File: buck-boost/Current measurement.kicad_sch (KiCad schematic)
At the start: 15 parts, among them U3 ACS712ELCTR-20A, U8 ACS730xLCTR-20AB, U9 ACS712ELCTR-20A

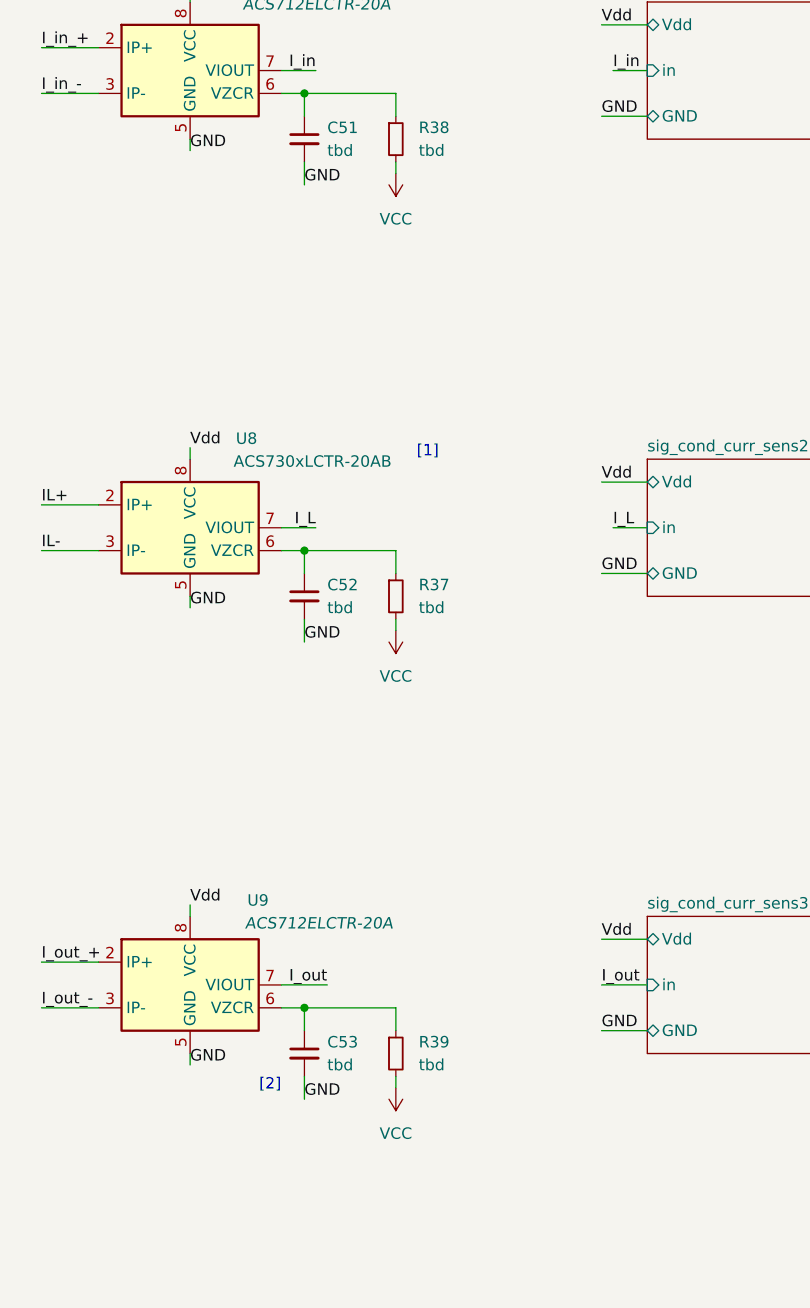
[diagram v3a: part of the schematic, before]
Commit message: Some errors in the schematics were corrected. PCB file V1.0
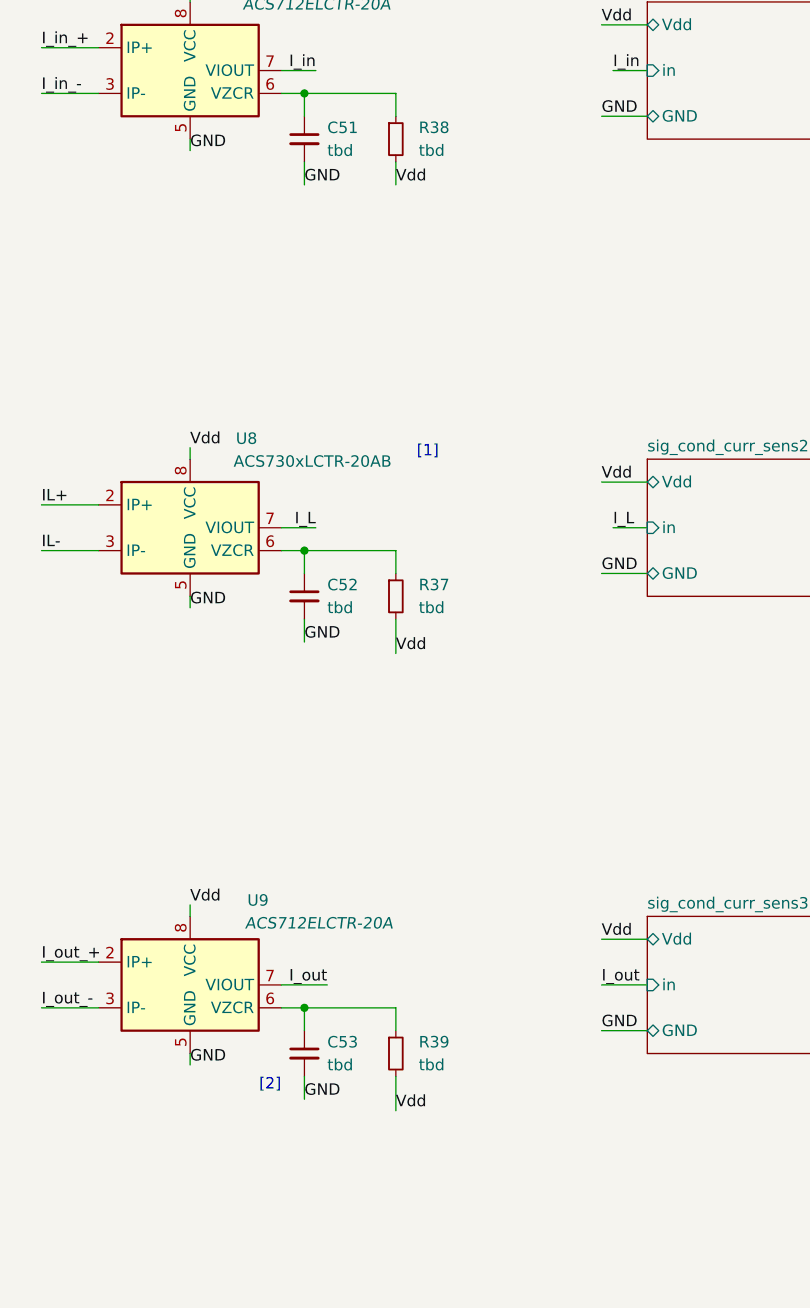
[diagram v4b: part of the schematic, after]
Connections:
- net VCC is gone; now on net Vdd: R37.2, R38.2, R39.2
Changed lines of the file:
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@@
-	(wire
-		(pts
-			(xy 116.84 142.24) (xy 116.84 143.51)
-		)
-		(stroke
-			(width 0)
-			(type default)
-		)
-	)
 	(wire
 		(pts
@@
 	(wire
 		(pts
-			(xy 116.84 91.44) (xy 116.84 92.71)
+			(xy 116.84 91.44) (xy 116.84 95.25)
 		)
 		(stroke
@@
 	(wire
 		(pts
+			(xy 116.84 142.24) (xy 116.84 146.05)
+		)
+		(stroke
+			(width 0)
+			(type default)
+		)
+	)
+	(wire
+		(pts
 			(xy 39.37 85.09) (xy 50.8 85.09)
 		)
@@
 	(wire
 		(pts
-			(xy 116.84 40.64) (xy 116.84 41.91)
+			(xy 116.84 40.64) (xy 116.84 43.18)
 		)
 		(stroke
@@
 		)
 	)
+	(label "Vdd"
+		(at 116.84 43.18 0)
+		(fields_autoplaced yes)
+		(effects
+			(font
+				(size 1.27 1.27)
+			)
+			(justify left bottom)
+		)
+	)
 	(label "IL_sens"
 		(at 74.93 180.34 0)
@@
 	(label "I_in_+"
 		(at 50.8 177.8 0)
+		(fields_autoplaced yes)
+		(effects
+			(font
+				(size 1.27 1.27)
+			)
+			(justify left bottom)
+		)
+	)
+	(label "Vdd"
+		(at 116.84 146.05 0)
+		(fields_autoplaced yes)
+		(effects
+			(font
+				(size 1.27 1.27)
+			)
+			(justify left bottom)
+		)
+	)
+	(label "Vdd"
+		(at 116.84 95.25 0)
 		(fields_autoplaced yes)
 		(effects
@@
 				(path "/3f994017-d36f-4c43-a8c8-740bd919e8ad/70cf8e5f-42f7-4af1-be5f-f7a395e09e78/4c95cbf9-e4e0-409d-a846-0f8d58b8f8d6"
 					(reference "R39")
-					(unit 1)
-				)
-			)
-		)
-	)
-	(symbol
-		(lib_id "power:VCC")
-		(at 116.84 92.71 180)
-		(unit 1)
-		(exclude_from_sim no)
-		(in_bom yes)
-		(on_board yes)
-		(dnp no)
-		(fields_autoplaced yes)
-		(property "Reference" "#PWR024"
-			(at 116.84 88.9 0)
-			(effects
-				(font
-					(size 1.27 1.27)
-				)
-				(hide yes)
-			)
-		)
-		(property "Value" "VCC"
-			(at 116.84 97.79 0)
-			(effects
-				(font
-					(size 1.27 1.27)
-				)
-			)
-		)
-		(property "Footprint" ""
-			(at 116.84 92.71 0)
-			(effects
-				(font
-					(size 1.27 1.27)
-				)
-				(hide yes)
-			)
-		)
-		(property "Datasheet" ""
-			(at 116.84 92.71 0)
-			(effects
-				(font
-					(size 1.27 1.27)
-				)
-				(hide yes)
-			)
-		)
-		(property "Description" "Power symbol creates a global label with name \"VCC\""
-			(at 116.84 92.71 0)
-			(effects
-				(font
-					(size 1.27 1.27)
-				)
-				(hide yes)
-			)
-		)
-		(pin "1"
-		)
-		(instances
-			(project "buck-boost-xp"
-				(path "/3f994017-d36f-4c43-a8c8-740bd919e8ad/70cf8e5f-42f7-4af1-be5f-f7a395e09e78/4c95cbf9-e4e0-409d-a846-0f8d58b8f8d6"
-					(reference "#PWR024")
 					(unit 1)
 				)
@@
 					(unit 1)
 				)
-			)
-		)
-	)
-	(symbol
-		(lib_id "power:VCC")
-		(at 116.84 41.91 180)
-		(unit 1)
-		(exclude_from_sim no)
-		(in_bom yes)
-		(on_board yes)
-		(dnp no)
-		(fields_autoplaced yes)
-		(property "Reference" "#PWR022"
-			(at 116.84 38.1 0)
-			(effects
-				(font
-					(size 1.27 1.27)
-				)
-				(hide yes)
-			)
-		)
-		(property "Value" "VCC"
-			(at 116.84 46.99 0)
-			(effects
-				(font
-					(size 1.27 1.27)
-				)
-			)
-		)
-		(property "Footprint" ""
-			(at 116.84 41.91 0)
-			(effects
-				(font
-					(size 1.27 1.27)
-				)
-				(hide yes)
-			)
-		)
-		(property "Datasheet" ""
-			(at 116.84 41.91 0)
-			(effects
-				(font
-					(size 1.27 1.27)
-				)
-				(hide yes)
-			)
-		)
-		(property "Description" "Power symbol creates a global label with name \"VCC\""
-			(at 116.84 41.91 0)
-			(effects
-				(font
-					(size 1.27 1.27)
-				)
-				(hide yes)
-			)
-		)
-		(pin "1"
-		)
-		(instances
-			(project "buck-boost-xp"
-				(path "/3f994017-d36f-4c43-a8c8-740bd919e8ad/70cf8e5f-42f7-4af1-be5f-f7a395e09e78/4c95cbf9-e4e0-409d-a846-0f8d58b8f8d6"
-					(reference "#PWR022")
-					(unit 1)
-				)
-			)
-		)
-	)
-	(symbol
-		(lib_id "power:VCC")
-		(at 116.84 143.51 180)
-		(unit 1)
-		(exclude_from_sim no)
-		(in_bom yes)
-		(on_board yes)
-		(dnp no)
-		(fields_autoplaced yes)
-		(property "Reference" "#PWR026"
-			(at 116.84 139.7 0)
-			(effects
-				(font
-					(size 1.27 1.27)
-				)
-				(hide yes)
-			)
-		)
-		(property "Value" "VCC"
-			(at 116.84 148.59 0)
-			(effects
-				(font
-					(size 1.27 1.27)
-				)
-			)
-		)
-		(property "Footprint" ""
-			(at 116.84 143.51 0)
-			(effects
-				(font
-					(size 1.27 1.27)
-				)
-				(hide yes)
-			)
-		)
-		(property "Datasheet" ""
-			(at 116.84 143.51 0)
-			(effects
-				(font
-					(size 1.27 1.27)
-				)
-				(hide yes)
-			)
-		)
-		(property "Description" "Power symbol creates a global label with name \"VCC\""
-			(at 116.84 143.51 0)
-			(effects
-				(font
-					(size 1.27 1.27)
-				)
-				(hide yes)
-			)
-		)
-		(pin "1"
-		)
-		(instances
-			(project "buck-boost-xp"
-				(path "/3f994017-d36f-4c43-a8c8-740bd919e8ad/70cf8e5f-42f7-4af1-be5f-f7a395e09e78/4c95cbf9-e4e0-409d-a846-0f8d58b8f8d6"
-					(reference "#PWR026")
-					(unit 1)
-				)
